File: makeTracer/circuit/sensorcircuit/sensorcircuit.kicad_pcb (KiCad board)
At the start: 2 copper layers, 90 x 70 mm, 38 parts, among them J1 Maincircuit, U1 LBR-127HLD, U2 RPR-220, U3 4052, U4 RPR-220, U5 LBR-127HLD, U6 LBR-127HLD, U7 LBR-127HLD, U8 LBR-127HLD, U9 LBR-127HLD

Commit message: ohsaycanyouwip
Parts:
- moved J1 48.5 mm to (58.6, 97.0)
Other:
- board size 90 x 70 mm -> 90 x 80.1 mm
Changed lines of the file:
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@@
   )
   (footprint "D4jikkenLibrary:RPR-220" (layer "F.Cu")
-    (at 79.2125 46.9625)
+    (at 79.2125 47)
     (property "Sheetfile" "sensorcircuit.kicad_sch")
     (property "Sheetname" "")
@@
   )
   (footprint "SamacSys:SHDR6W69P0X250_1X6_1500X490X1040P" (layer "F.Cu")
-    (at 58.65 48.45)
+    (at 58.65 96.95)
     (descr "171825-6")
     (tags "Connector")
@@
     (pad "" np_thru_hole circle (at 0 0) (size 3.2 3.2) (drill 3.2) (layers "F&B.Cu" "*.Mask"))
   )
+  (gr_line (start 39.5 91) (end 40.5 92.5)
+    (stroke (width 0.1) (type default)) (layer "Edge.Cuts"))
   (gr_line (start 52.5 85) (end 77.5 85)
     (stroke (width 0.1) (type default)) (layer "Edge.Cuts"))
@@
   (gr_line (start 20 87.5) (end 20 22.5)
     (stroke (width 0.1) (type default)) (layer "Edge.Cuts"))
+  (gr_line (start 22.5 90) (end 37.5 90)
+    (stroke (width 0.1) (type default)) (layer "Edge.Cuts"))
+  (gr_line (start 40.5 92.5) (end 44.5 98.5)
+    (stroke (width 0.1) (type default)) (layer "Edge.Cuts"))
   (gr_line (start 80 82.5) (end 80 57.5)
     (stroke (width 0.1) (type default)) (layer "Edge.Cuts"))
   (gr_arc (start 110 87.5) (mid 109.267767 89.267767) (end 107.5 90)
     (stroke (width 0.1) (type default)) (layer "Edge.Cuts"))
+  (gr_arc (start 90.5 91) (mid 91.381966 90.263932) (end 92.5 90)
+    (stroke (width 0.1) (type default)) (layer "Edge.Cuts"))
   (gr_line (start 50 57.5) (end 50 82.5)
     (stroke (width 0.1) (type default)) (layer "Edge.Cuts"))
+  (gr_line (start 89.5 92.5) (end 85.5 98.5)
+    (stroke (width 0.1) (type default)) (layer "Edge.Cuts"))
+  (gr_arc (start 85.5 98.5) (mid 84.201308 99.678923) (end 82.5 100.105551)
+    (stroke (width 0.1) (type default)) (layer "Edge.Cuts"))
   (gr_line (start 107.5 20) (end 22.5 20)
     (stroke (width 0.1) (type default)) (layer "Edge.Cuts"))
   (gr_arc (start 80 82.5) (mid 79.267767 84.267767) (end 77.5 85)
     (stroke (width 0.1) (type default)) (layer "Edge.Cuts"))
-  (gr_line (start 107.5 90) (end 22.5 90)
+  (gr_arc (start 47.5 100.105551) (mid 45.798692 99.678923) (end 44.5 98.5)
     (stroke (width 0.1) (type default)) (layer "Edge.Cuts"))
   (gr_line (start 110 87.5) (end 110 22.5)
+    (stroke (width 0.1) (type default)) (layer "Edge.Cuts"))
+  (gr_arc (start 37.5 90) (mid 38.618034 90.263932) (end 39.5 91)
+    (stroke (width 0.1) (type default)) (layer "Edge.Cuts"))
+  (gr_line (start 92.5 90) (end 107.5 90)
+    (stroke (width 0.1) (type default)) (layer "Edge.Cuts"))
+  (gr_line (start 82.5 100.105551) (end 47.5 100.105551)
+    (stroke (width 0.1) (type default)) (layer "Edge.Cuts"))
+  (gr_line (start 90.5 91) (end 89.5 92.5)
     (stroke (width 0.1) (type default)) (layer "Edge.Cuts"))
   (gr_arc (start 22.5 90) (mid 20.732233 89.267767) (end 20 87.5)
@@
     (stroke (width 0.1) (type default)) (layer "F.Fab"))
   (dimension (type aligned) (layer "Edge.Cuts")
+    (pts (xy 65 100.105551) (xy 65 90))
+    (height 51.5)
+    (gr_text "10.1056 mm" (at 115.35 95.052775 90) (layer "Edge.Cuts")
+      (effects (font (size 1 1) (thickness 0.15)))
+    )
+    (format (prefix "") (suffix "") (units 3) (units_format 1) (precision 4))
+    (style (thickness 0.1) (arrow_length 1.27) (text_position_mode 0) (extension_height 0.58642) (extension_offset 0.5) keep_text_aligned)
+  )
+  (dimension (type aligned) (layer "Edge.Cuts")
     (pts (xy 65 55) (xy 65 20))
     (height 63.5)
@@
       (effects (font (size 1 1) (thickness 0.15)))
     )
+    (format (prefix "") (suffix "") (units 3) (units_format 1) (precision 4))
+    (style (thickness 0.1) (arrow_length 1.27) (text_position_mode 0) (extension_height 0.58642) (extension_offset 0.5) keep_text_aligned)
+  )
+  (dimension (type aligned) (layer "Edge.Cuts")
+    (pts (xy 65 85) (xy 65 95))
+    (height -88)
+    (gr_text "10.0000 mm" (at 151.85 90 90) (layer "Edge.Cuts")
+      (effects (font (size 1 1) (thickness 0.15)))
+    )

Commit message: complete: circuit
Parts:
- J1, R1, R10, R11, R12, R13, R14, R15, R16, R2, R3, R4, R5, R6, R7, R8, R9, RV1, RV2, RV3, RV4, RV5, RV6, RV7, RV8, U3: moved to B.Cu
- moved U6 78.1 mm to (93.8, 29.3), turned to 90 degrees
- moved RV1 74.4 mm to (93.0, 55.2), turned to -90 degrees
- moved U7 73.0 mm to (84.8, 29.3), turned to 90 degrees
- moved R2 64.8 mm to (95.5, 51.8), turned to 90 degrees
- moved R10 60.6 mm to (100.0, 34.8), turned to 90 degrees
- moved R12 59.8 mm to (100.0, 46.3), turned to 90 degrees
- moved R4 56.3 mm to (85.2, 44.5)
- moved RV2 56.2 mm to (83.5, 48.2), turned to -90 degrees
- moved R9 52.5 mm to (91.5, 30.5), turned to 90 degrees
- moved RV5 51.9 mm to (103.2, 37.0)
- moved U9 51.4 mm to (31.8, 29.3), turned to 90 degrees
- moved RV8 47.6 mm to (26.8, 43.0), turned to 180 degrees
- moved R11 47.5 mm to (82.5, 30.5), turned to 90 degrees
- moved R1 46.4 mm to (75.3, 33.5), turned to 180 degrees
- moved U8 46.0 mm to (40.8, 29.3), turned to 90 degrees
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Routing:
- net VDD: track 0.00 -> 244.1 mm, vias 0 -> 7
- net /Ann_1: track 0.00 -> 76.1 mm, vias 0 -> 2
- net GND: track 0.00 -> 75.9 mm, vias 0 -> 20
- net /Dig_0: track 0.00 -> 69.8 mm, vias 0 -> 2
- net /Ann_3: track 0.00 -> 68.9 mm, vias 0 -> 2
- net /Dig_1: track 0.00 -> 67.2 mm, vias 0 -> 2
- net /Dig_3: track 0.00 -> 65.7 mm, vias 0 -> 2
- net /Dig_2: track 0.00 -> 59.7 mm, vias 0 -> 2
- net /Ann_0: track 0.00 -> 55.6 mm
- net /Ann_2: track 0.00 -> 49.4 mm, vias 0 -> 2
- net Digital_Process: track 0.00 -> 38.5 mm, vias 0 -> 2
- net Net-(R1-Pad2): track 0.00 -> 14.4 mm
- net Net-(R8-Pad1): track 0.00 -> 11.1 mm
- net Net-(R14-Pad1): track 0.00 -> 8.84 mm
- net Port_SEL2: track 0.00 -> 7.83 mm
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- added copper zone on B.Cu, net GND
- added copper zone on B.Cu, net VDD
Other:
- board size 90 x 80.1 mm -> 90 x 40 mm
- board text added: "FRONTSIDE"
- board text added: "LINE WIDTH"

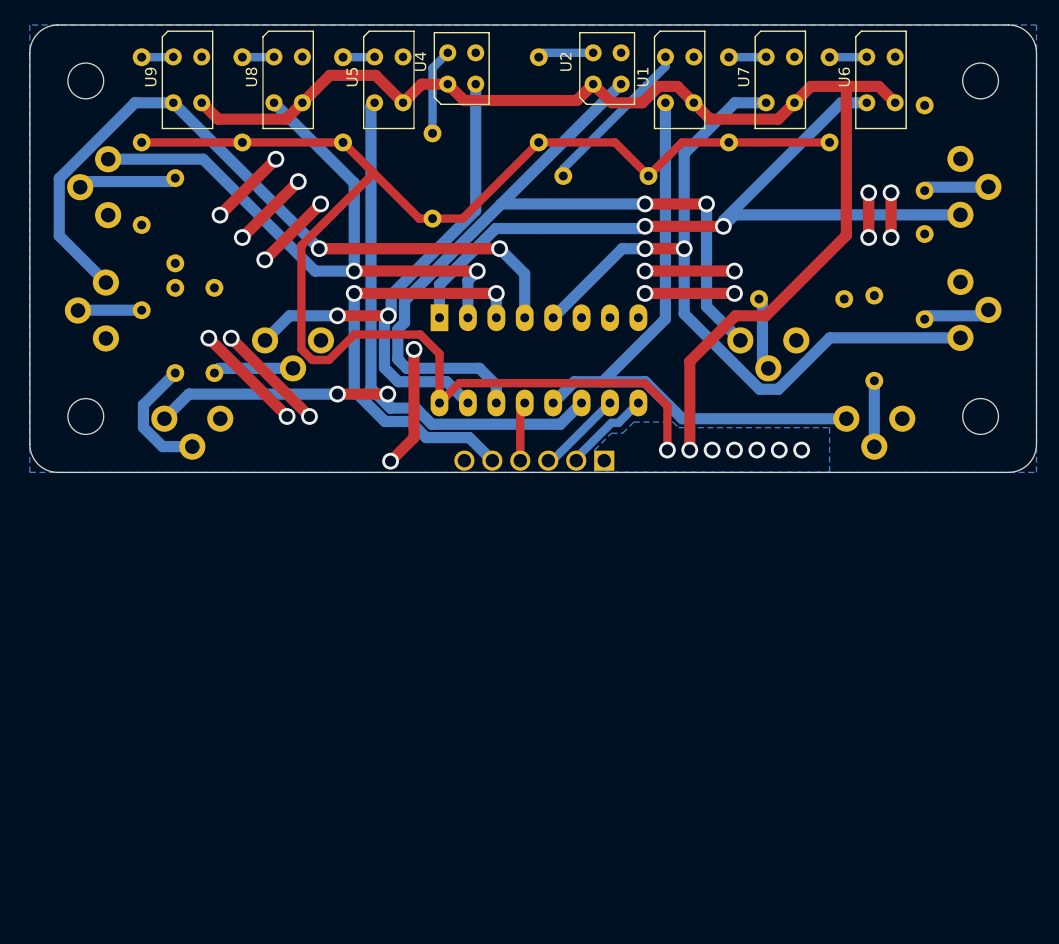
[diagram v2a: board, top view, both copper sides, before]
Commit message: fix: .2mm to .4mm
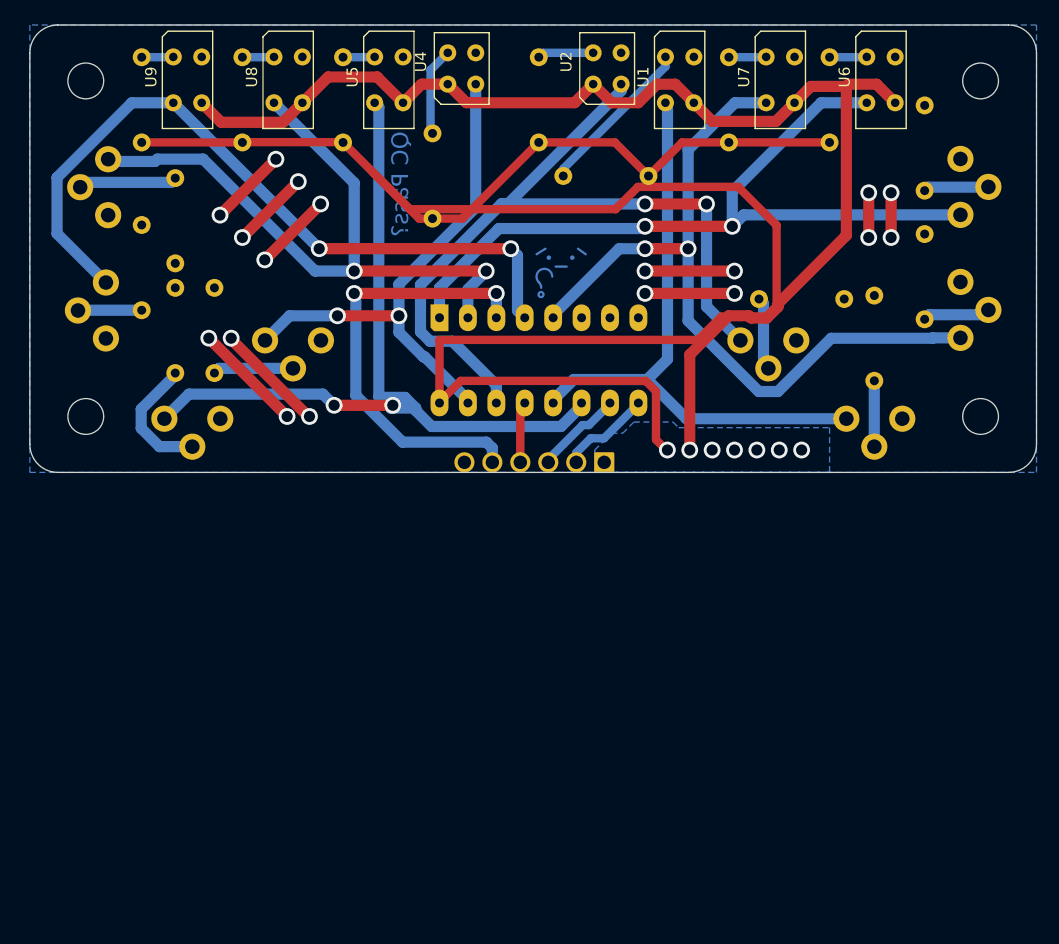
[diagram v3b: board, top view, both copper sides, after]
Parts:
- moved J1 0.15 mm to (71.3, 59.1)
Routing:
- net VDD: track 244.1 -> 292.7 mm
- net GND: track 75.9 -> 65.1 mm, vias 20 -> 18
- net /Ann_1: track 76.1 -> 72.1 mm
- net /Ann_3: track 68.9 -> 72.6 mm
- net /Ann_2: track 49.4 -> 46.9 mm
- net /Ann_0: track 55.6 -> 54.3 mm
- net /Dig_2: track 59.7 -> 61.0 mm
- net Digital_Process: track 38.5 -> 39.5 mm
- net /Dig_3: track 65.7 -> 66.6 mm
- net Port_SEL2: track 7.83 -> 8.53 mm
- net /Dig_0: track 69.8 -> 70.4 mm
- net /Dig_1: track 67.2 -> 67.8 mm
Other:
- board text added: "QC Pass?"
